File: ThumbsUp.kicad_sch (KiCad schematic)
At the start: 56 parts, among them J1 52559-1233, J1L1 PJ-3200B, J1R1 PJ-3200B, J2 52559-1233, U1 ProMicro

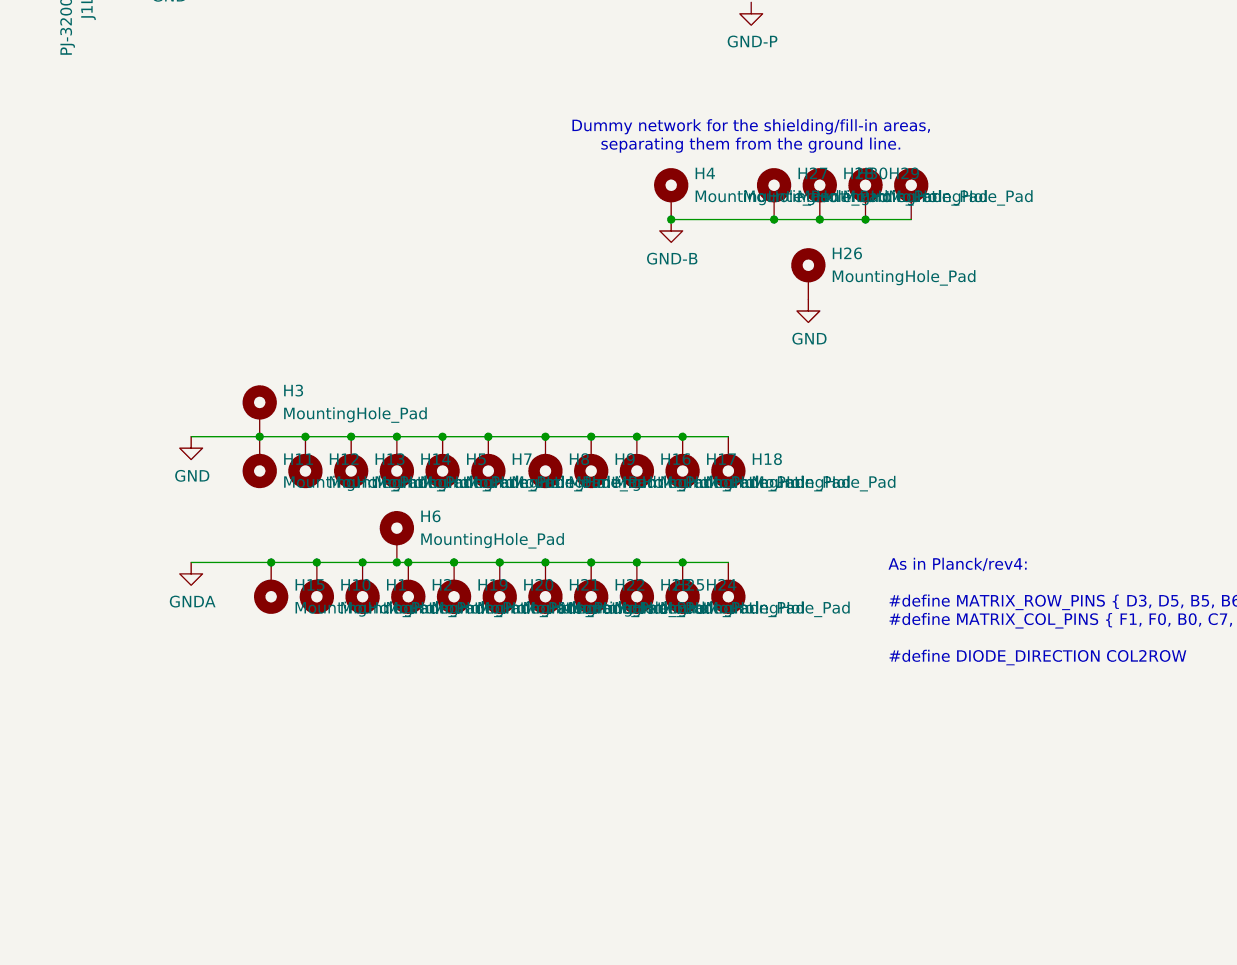
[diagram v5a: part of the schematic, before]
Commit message: v12: Added stand-offs instead of pin headers/sockets.
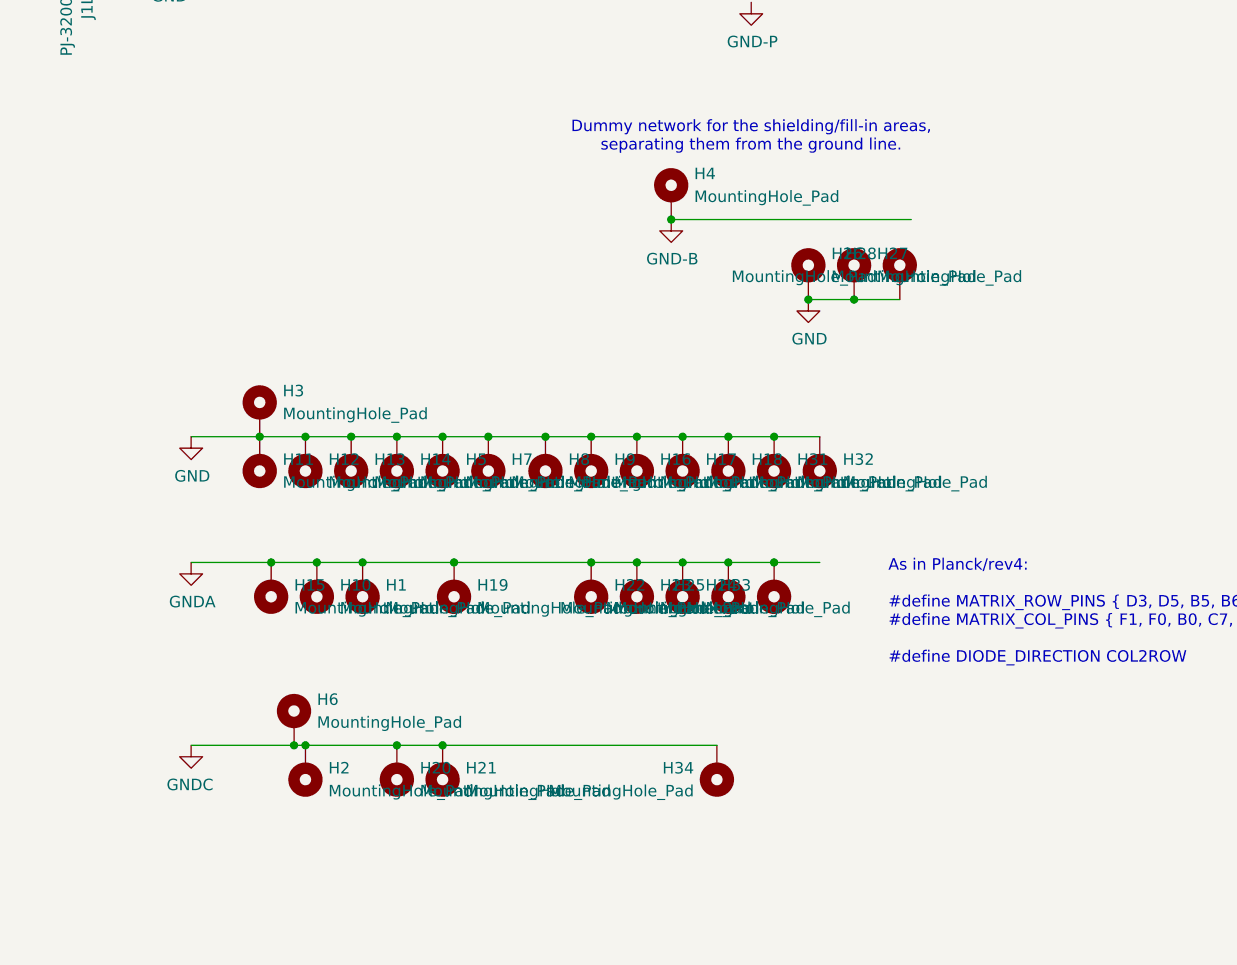
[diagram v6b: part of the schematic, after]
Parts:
- removed H29, H30: MountingHole_Pad, MountingHole:MountingHole_4.5mm_Pad, symbol Mechanical:MountingHole_Pad
- added H31, H32, H33, H34: MountingHole_Pad, MountingHole:MountingHole_3.5mm_Pad, symbol Mechanical:MountingHole_Pad
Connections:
- net GND: now also H27.1, H28.1, H31.1, H32.1
- net GND-B: no longer H27.1, H28.1
- net GNDA: now also H33.1; no longer H2.1, H20.1, H21.1, H6.1
- new net GNDC: H2.1, H20.1, H21.1, H34.1, H6.1
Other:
- moved on the sheet: H2, H20, H21, H27, H28, H6

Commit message: v12: Minor corrections.
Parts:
- removed H26, H28: MountingHole_Pad, MountingHole:MountingHole_4.5mm_Pad, symbol Mechanical:MountingHole_Pad
- H27: footprint MountingHole:MountingHole_4.5mm_Pad -> MountingHole:MountingHole_3.5mm_Pad
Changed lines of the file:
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@@
 	)
 	(junction
-		(at 477.52 262.89)
-		(diameter 0)
-		(color 0 0 0 0)
-	)
-	(junction
 		(at 438.15 207.01)
 		(diameter 0)
@@
 	(symbol
 		(lib_id "Mechanical:MountingHole_Pad")
-		(at 487.68 260.35 0)
-		(mirror y)
-		(unit 1)
-		(exclude_from_sim no)
-		(in_bom no)
-		(on_board yes)
-		(dnp no)
-		(property "Reference" "H28"
-			(at 485.14 257.8099 0)
-			(effects
-				(font
-					(size 1.27 1.27)
-				)
-				(justify left)
-			)
-		)
-		(property "Value" "MountingHole_Pad"
-			(at 485.14 260.3499 0)
-			(effects
-				(font
-					(size 1.27 1.27)
-				)
-				(justify left)
-			)
-		)
-		(property "Footprint" "MountingHole:MountingHole_4.5mm_Pad"
-			(at 487.68 260.35 0)
-			(effects
-				(font
-					(size 1.27 1.27)
-				)
-				(hide yes)
-			)
-		)
-		(property "Datasheet" "~"
-			(at 487.68 260.35 0)
-			(effects
-				(font
-					(size 1.27 1.27)
-				)
-				(hide yes)
-			)
-		)
-		(property "Description" "Mounting Hole with connection"
-			(at 487.68 260.35 0)
-			(effects
-				(font
-					(size 1.27 1.27)
-				)
-				(hide yes)
-			)
-		)
-		(pin "1"
-		)
-		(instances
-			(project "ThumbsUp"
-				(path "/467ed76c-995a-4514-a2e9-81ed0f98430e"
-					(reference "H28")
-					(unit 1)
-				)
-			)
-		)
-	)
-	(symbol
-		(lib_id "Mechanical:MountingHole_Pad")
 		(at 436.88 280.67 180)
 		(unit 1)
@@
 	(symbol
 		(lib_id "Mechanical:MountingHole_Pad")
-		(at 477.52 260.35 0)
-		(unit 1)
-		(exclude_from_sim no)
-		(in_bom no)
-		(on_board yes)
-		(dnp no)
-		(fields_autoplaced yes)
-		(property "Reference" "H26"
-			(at 480.06 257.8099 0)
-			(effects
-				(font
-					(size 1.27 1.27)
-				)
-				(justify left)
-			)
-		)
-		(property "Value" "MountingHole_Pad"
-			(at 480.06 260.3499 0)
-			(effects
-				(font
-					(size 1.27 1.27)
-				)
-				(justify left)
-			)
-		)
-		(property "Footprint" "MountingHole:MountingHole_4.5mm_Pad"
-			(at 477.52 260.35 0)
-			(effects
-				(font
-					(size 1.27 1.27)
-				)
-				(hide yes)
-			)
-		)
-		(property "Datasheet" "~"
-			(at 477.52 260.35 0)
-			(effects
-				(font
-					(size 1.27 1.27)
-				)
-				(hide yes)
-			)
-		)
-		(property "Description" "Mounting Hole with connection"
-			(at 477.52 260.35 0)
-			(effects
-				(font
-					(size 1.27 1.27)
-				)
-				(hide yes)
-			)
-		)
-		(pin "1"
-		)
-		(instances
-			(project "ThumbsUp"
-				(path "/467ed76c-995a-4514-a2e9-81ed0f98430e"
-					(reference "H26")
-					(unit 1)
-				)
-			)
-		)
-	)
-	(symbol
-		(lib_id "Mechanical:MountingHole_Pad")
 		(at 420.37 309.88 0)
 		(unit 1)
@@
 			)
 		)
-		(property "Footprint" "MountingHole:MountingHole_4.5mm_Pad"
+		(property "Footprint" "MountingHole:MountingHole_3.5mm_Pad"
 			(at 482.6 260.35 0)
 			(effects
